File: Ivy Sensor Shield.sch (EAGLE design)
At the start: 12 parts

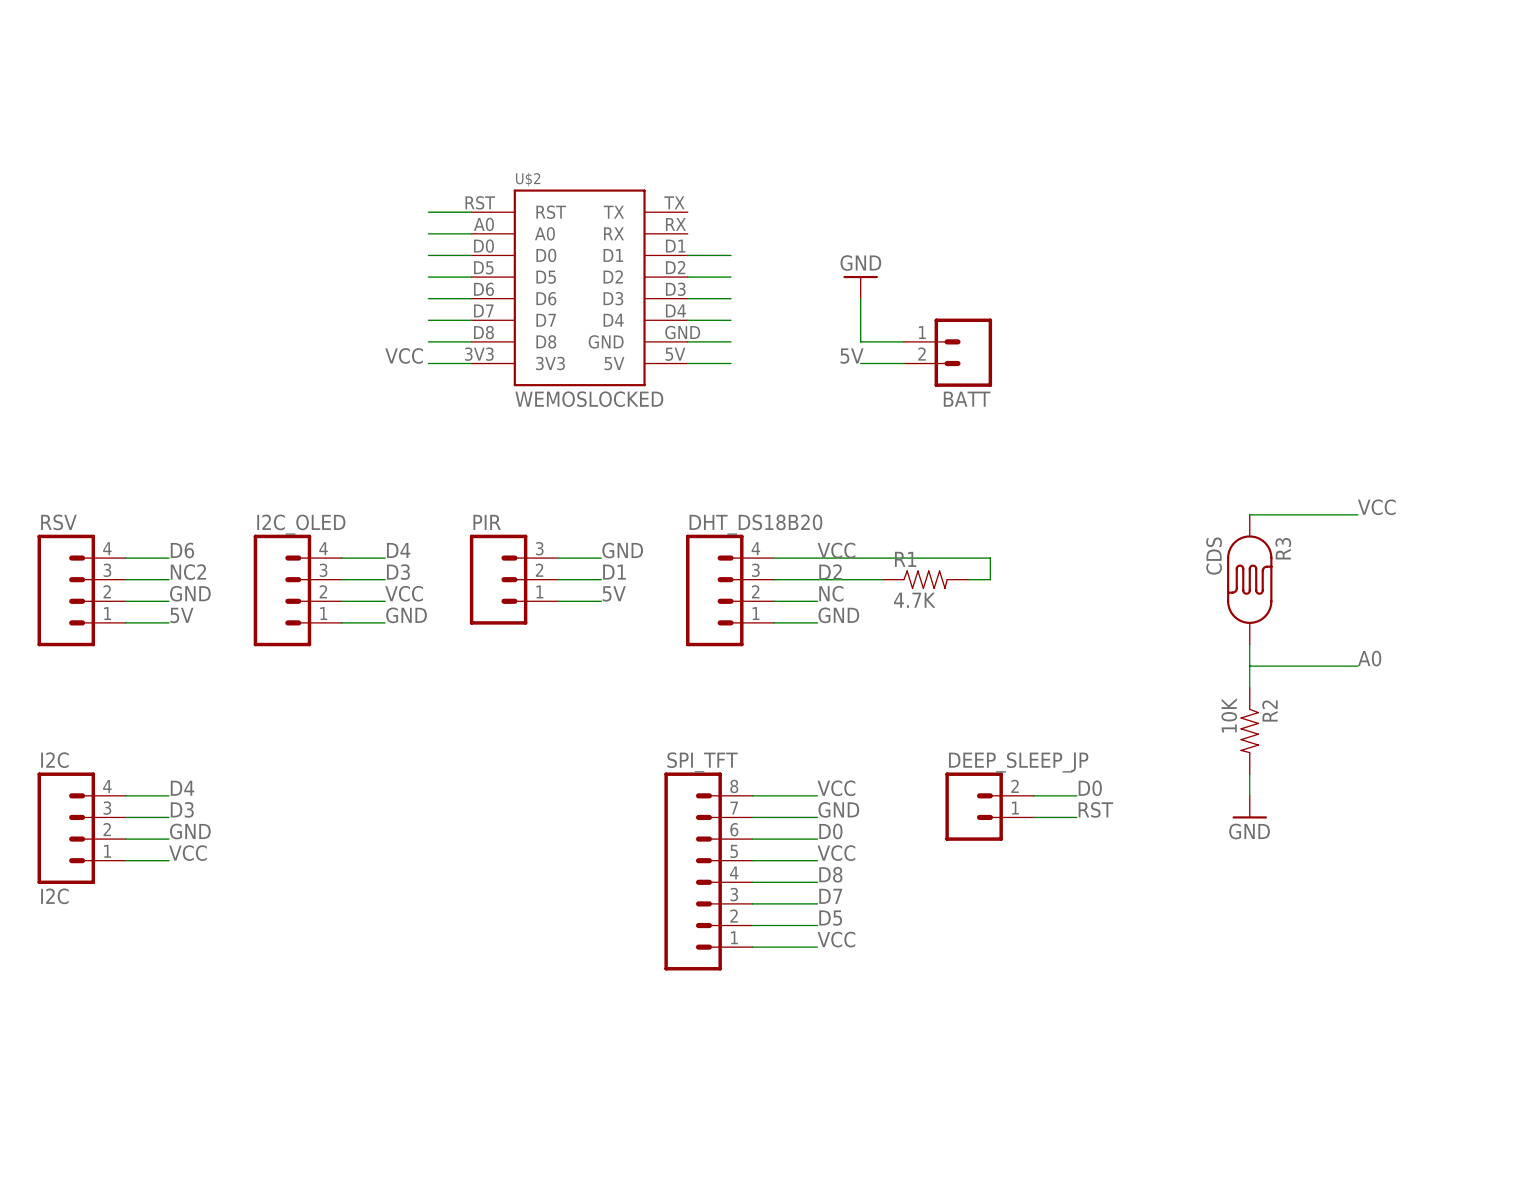
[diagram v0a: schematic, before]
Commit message: Update Sensor to version 0.2
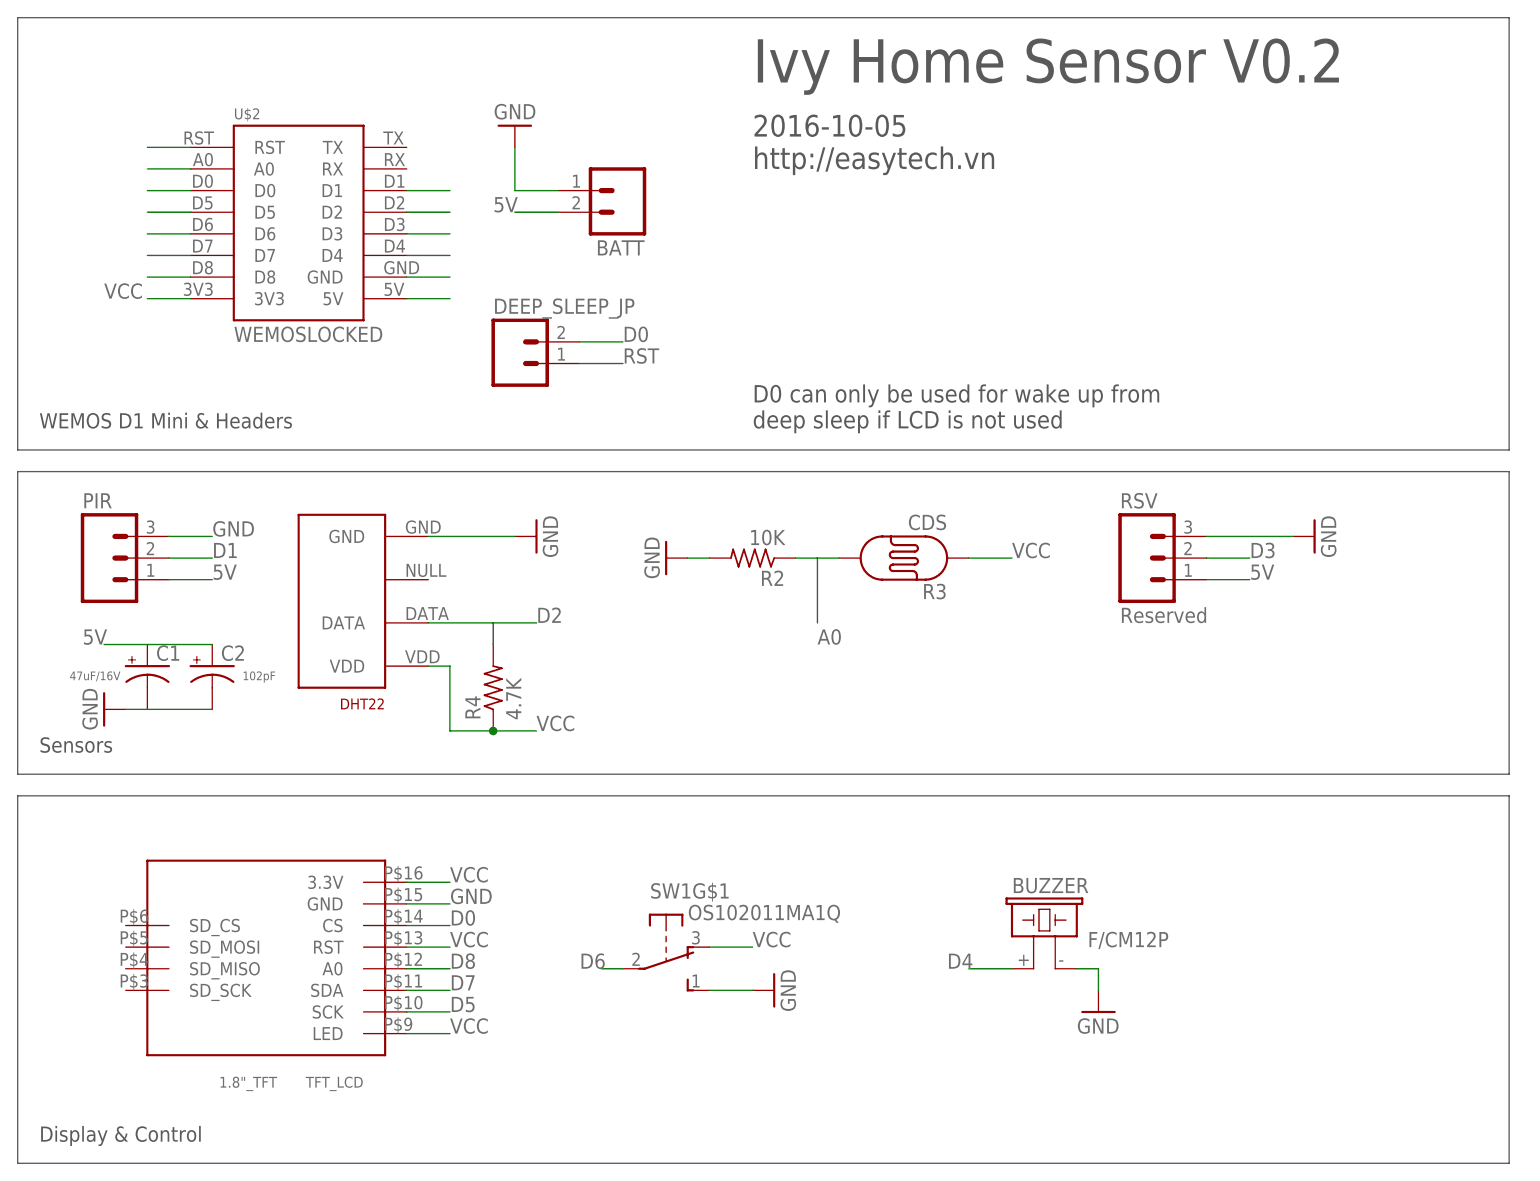
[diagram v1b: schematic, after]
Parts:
- removed DHT_DS18B20, I2C_OLED: (no value), SparkFun-Connectors:M04PTH
- removed I2C: I2C, SparkFun-Connectors:M04PTH
- removed R1: 4.7K, SparkFun-Passives:RESISTOR0805-RES
- removed SPI_TFT: (no value), SparkFun-Connectors:M08
- added BUZZER: F/CM12P, buzzer:F/CM12P
- added C1: 47uF/16V, SparkFun-Capacitors:CAP_POLPTH2
- added C2: 102pF, SparkFun-Capacitors:CAP_POLPTH2
- added DHT22: (no value), RHT03_DHT-22_AM2302:RHT03_DHT-22_AM2302RA
- added R4: 4.7K, resistor:R-US_R0805
- added SW1: OS102011MA1Q, adafruit:OS102011MA1Q
- added TFT_LCD: 1.8"_TFT, tft_1.8_1.44_oled_0.96:1.8"_TFT
- R2: device SparkFun-Passives:RESISTOR0805-RES -> resistor:R-US_R0805
- RSV: value (none) -> Reserved; device SparkFun-Connectors:M04PTH -> SparkFun-Connectors:M03PTH
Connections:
- removed net NC: DHT_DS18B20.2
- removed net NC2: RSV.3
- net 5V: now also C1.+, C2.+
- net D0: now also TFT_LCD.CS; no longer SPI_TFT.6
- net D2: now also DHT22.DATA, R4.2; no longer DHT_DS18B20.3, R1.1
- net D3: now also RSV.2; no longer I2C.3, I2C_OLED.3
- net D4: now also BUZZER.1; no longer I2C.4, I2C_OLED.4
- net D5: now also TFT_LCD.SCK; no longer SPI_TFT.2
- net D6: now also SW1G$1.P; no longer RSV.4
- net D7: now also TFT_LCD.SDA; no longer SPI_TFT.3
- net D8: now also TFT_LCD.A0; no longer SPI_TFT.4
- net GND: now also BUZZER.2, C1.-, C2.-, DHT22.GND, RSV.3, SW1G$1.S, TFT_LCD.GND; no longer DHT_DS18B20.1, I2C.2, I2C_OLED.1, RSV.2, SPI_TFT.7
- net VCC: now also DHT22.VDD, R4.1, SW1G$1.O, TFT_LCD.3.3V, TFT_LCD.LED, TFT_LCD.RST; no longer DHT_DS18B20.4, I2C.1, I2C_OLED.2, R1.2, SPI_TFT.1, SPI_TFT.5, SPI_TFT.8
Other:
- note added: "2016-10-05 http://easytech.vn"
- note added: "D0 can only be used for wake up from deep sleep if LCD is not used"
- note added: "Display & Control"
- note added: "Ivy Home Sensor V0.2"
- note added: "Sensors"
- note added: "WEMOS D1 Mini & Headers"
- moved on the sheet: BATT, DEEP_SLEEP_JP, PIR, R2, R3, U$2
